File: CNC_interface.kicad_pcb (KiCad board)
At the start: 2 copper layers, 21 parts, among them J1 Conn_01x04_Male, J10 Conn_01x08, J11 Conn_01x08, J12 Conn_01x08, J13 Conn_01x08, J14 Conn_01x03_Male, J15 Conn_01x03_Male, J16 Conn_01x03_Male, J2 Conn_01x04_Male, J3 Conn_01x04_Male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

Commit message: adding capacitance footprints
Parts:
- added C1: CP, Capacitor_THT:CP_Radial_D8.0mm_P3.50mm, F.Cu at (214.6, 97.8)
- added C2: CP, Capacitor_THT:CP_Radial_D10.0mm_P5.00mm, F.Cu at (203.1, 98.8)

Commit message: Groupage drivers
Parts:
- moved J8 3.86 mm to (234.9, 69.9)
- moved J10 3.86 mm to (234.9, 95.9)
- moved J12 3.86 mm to (234.9, 121.3)
- moved J9 0.65 mm to (247.7, 69.9)
- moved J11 0.64 mm to (247.7, 95.9)
- moved J13 0.64 mm to (247.7, 121.3)
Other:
- net class Default removed

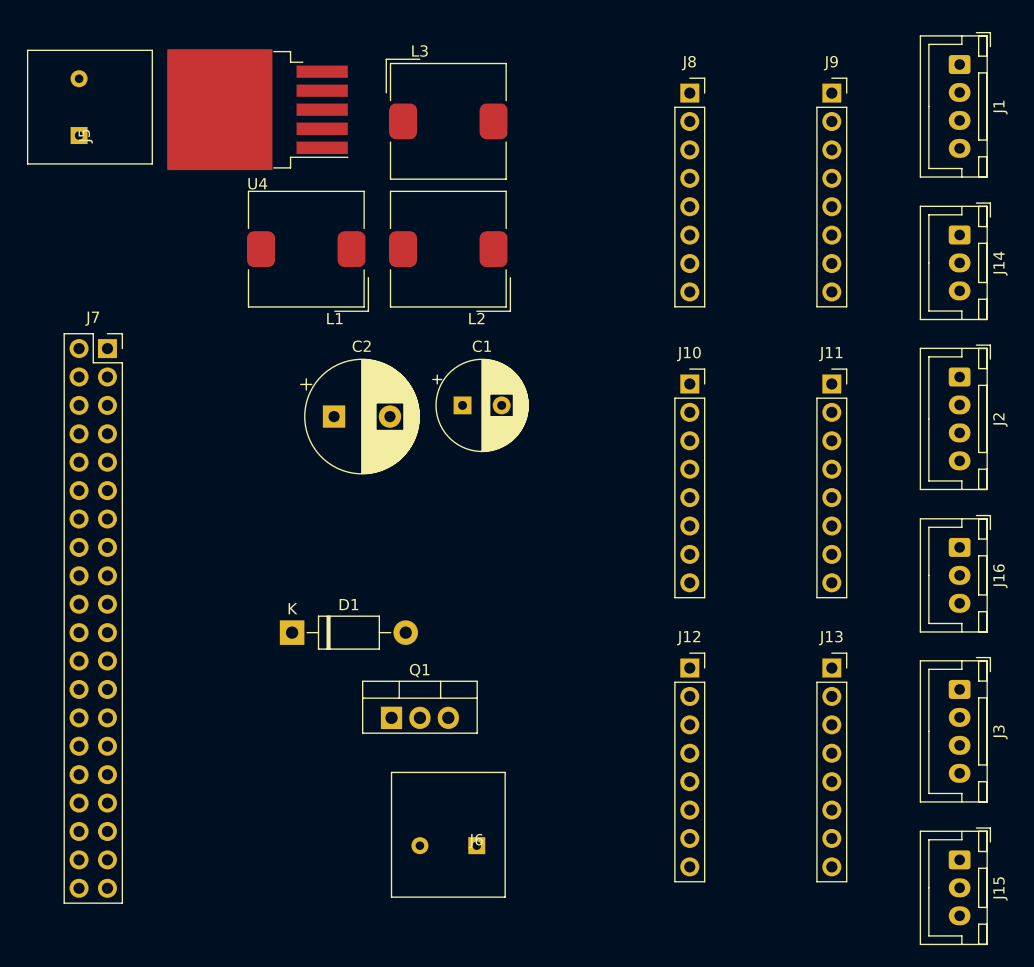
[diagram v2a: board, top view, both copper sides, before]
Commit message: Placing components on PCB
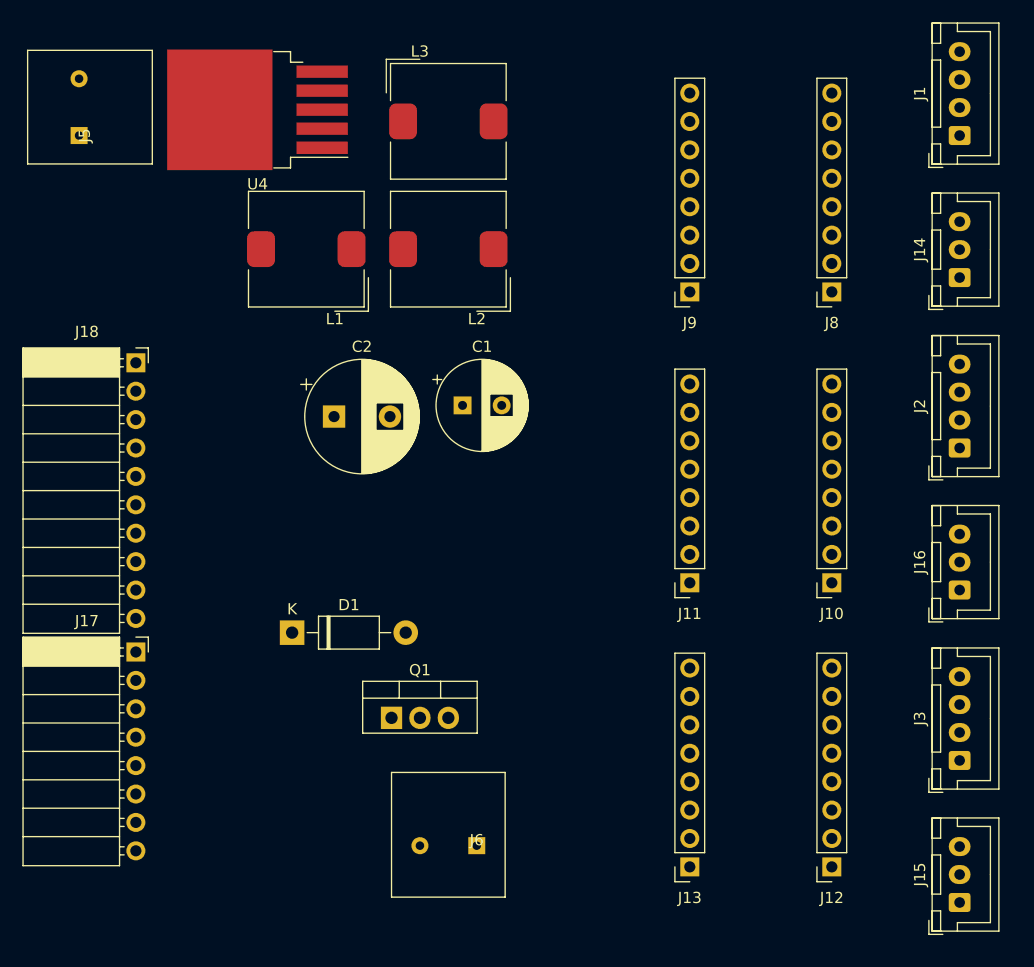
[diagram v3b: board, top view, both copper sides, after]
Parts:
- removed J7: Conn_02x20_Odd_Even, Connector_PinSocket_2.54mm:PinSocket_2x20_P2.54mm_Vertical
- added J17: Conn_01x08, Connector_PinSocket_2.54mm:PinSocket_1x08_P2.54mm_Horizontal, F.Cu at (185.4, 119.8)
- added J18: Conn_01x10, Connector_PinSocket_2.54mm:PinSocket_1x10_P2.54mm_Horizontal, F.Cu at (185.4, 94.0)
- moved J10 21.8 mm to (247.7, 113.7), turned to 180 degrees
- moved J11 21.8 mm to (234.9, 113.7), turned to 180 degrees
- moved J12 21.8 mm to (247.7, 139.1), turned to 180 degrees
- moved J13 21.8 mm to (234.9, 139.1), turned to 180 degrees
- moved J8 21.8 mm to (247.7, 87.6), turned to 180 degrees
- moved J9 21.8 mm to (234.9, 87.6), turned to 180 degrees
- moved J1 6.35 mm to (259.1, 73.7), turned to 90 degrees
- moved J2 6.35 mm to (259.1, 101.6), turned to 90 degrees
- moved J3 6.35 mm to (259.1, 129.5), turned to 90 degrees
- moved J14 3.81 mm to (259.1, 86.4), turned to 90 degrees
- moved J15 3.81 mm to (259.1, 142.2), turned to 90 degrees
- moved J16 3.81 mm to (259.1, 114.3), turned to 90 degrees
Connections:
- J1 pad 1: x1 -> OB2x
- J1 pad 2: x2 -> OB1x
- J1 pad 3: x3 -> OA1x
- J1 pad 4: x4 -> OA2x
- J10 pad 2: VIOy -> +5V
- J10 pad 8: VMy -> DC+
- J12 pad 2: VIOz -> +5V
- J12 pad 8: VMz -> DC+
- J2 pad 1: y1 -> OB2y
- J2 pad 2: y2 -> OB1y
- J2 pad 3: y3 -> OA1y
- J2 pad 4: y4 -> OA2y
- J3 pad 1: z1 -> OB2z
- J3 pad 2: z2 -> OB1z
- J3 pad 3: z3 -> OA1z
- J3 pad 4: z4 -> OA2z
- J8 pad 2: VIOx -> +5V
- J8 pad 8: VMx -> DC+

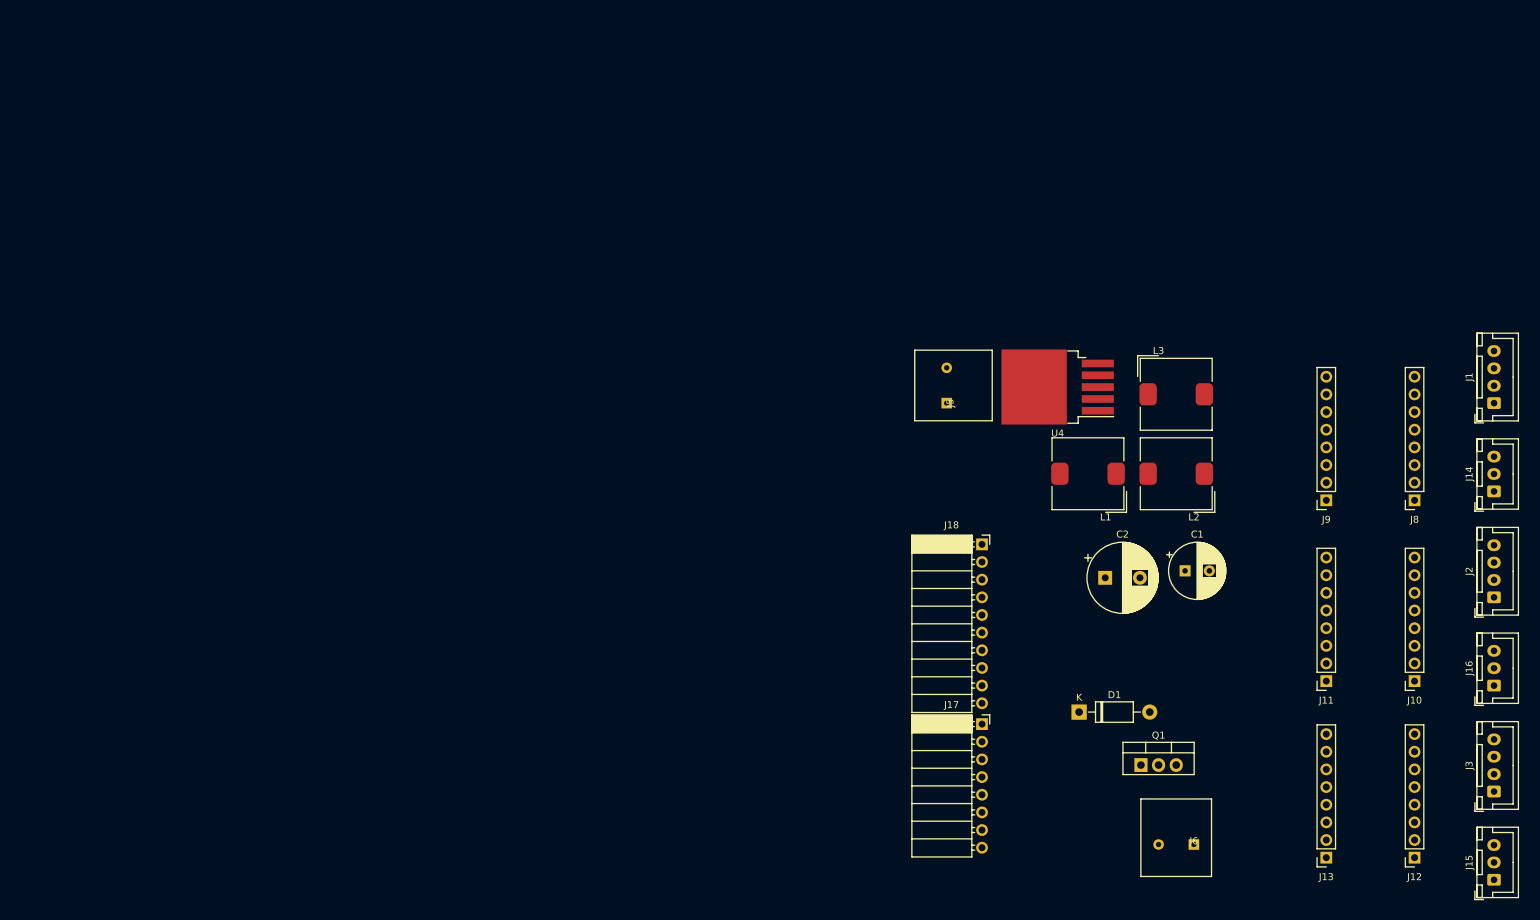
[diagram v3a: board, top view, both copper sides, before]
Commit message: wiring input to TMC
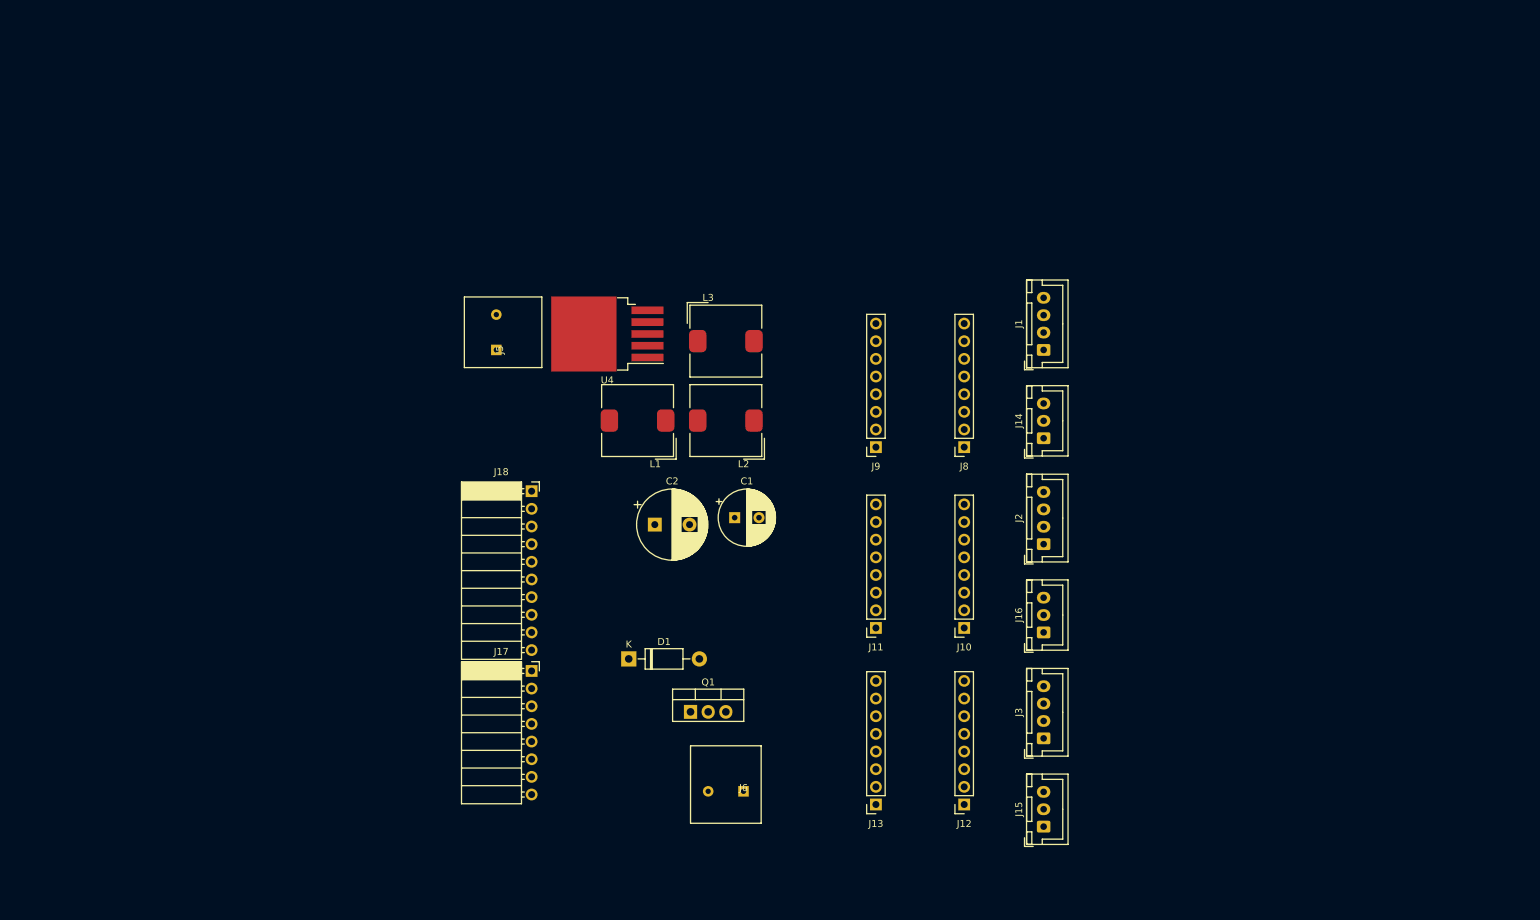
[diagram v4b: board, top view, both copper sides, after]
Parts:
- moved C2 65.2 mm to (138.3, 91.1)
- moved J10 65.2 mm to (182.9, 106.0)
- moved J12 65.2 mm to (182.9, 131.4)
- moved J6 65.2 mm to (151.1, 129.5)
- moved J8 65.2 mm to (182.9, 80.0)
- moved L2 65.2 mm to (148.6, 76.2)
- moved L3 65.2 mm to (148.6, 64.7)
- moved U4 65.2 mm to (131.5, 63.7)
- moved J5 65.2 mm to (115.5, 66.0)
- moved C1 65.2 mm to (149.8, 90.1)
- moved D1 65.2 mm to (134.6, 110.5)
- moved J1 65.2 mm to (194.3, 66.0)
- moved J11 65.2 mm to (170.2, 106.0)
- moved J13 65.2 mm to (170.2, 131.4)
- moved J14 65.2 mm to (194.3, 78.7)
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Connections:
- J11 pad 3: CLKy -> unconnected-(J11-Pad3)
- J11 pad 4: PDNUARTy -> unconnected-(J11-Pad4)
- J11 pad 5: PDNUARTy -> unconnected-(J11-Pad5)
- J13 pad 3: CLKz -> unconnected-(J13-Pad3)
- J13 pad 4: PDNUARTz -> unconnected-(J13-Pad4)
- J13 pad 5: PDNUARTz -> unconnected-(J13-Pad5)
- J17 pad 1: 7 -> ENy
- J17 pad 2: 6 -> STEPy
- J17 pad 3: 5 -> DIRy
- J17 pad 4: 4 -> ENx
- J17 pad 5: 3 -> STEPx
- J17 pad 6: 2 -> DIRx
- J18 pad 10: 8 -> DIRz
- J18 pad 6: 12 -> DCtrl
- J18 pad 8: 10 -> ENz
- J18 pad 9: 9 -> STEPz
- J9 pad 3: CLKx -> unconnected-(J9-Pad3)
- J9 pad 4: PDNUARTx -> unconnected-(J9-Pad4)
- J9 pad 5: PDNUARTx -> unconnected-(J9-Pad5)

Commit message: debut seance
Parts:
- added D2: D, Diode_THT:D_DO-201AD_P15.24mm_Horizontal, F.Cu at (119.3, 84.1)
- added J19: USB_C_Receptacle, Connector_USB:USB_C_Receptacle_Amphenol_12401548E4-2A_CircularHoles, F.Cu at (101.6, 113.6)
- moved J3 156.4 mm to (50.8, 59.8), turned to -90 degrees
- moved J1 150.6 mm to (50.8, 111.8), turned to -90 degrees
- moved J12 146.2 mm to (58.4, 54.6), turned to 0 degrees
- moved J2 143.8 mm to (50.8, 85.2), turned to -90 degrees
- moved J15 137.4 mm to (99.0, 35.6), turned to 180 degrees
- moved J6 132.3 mm to (50.8, 43.2), turned to 90 degrees
- moved J8 127.2 mm to (58.4, 106.7), turned to 0 degrees
- moved J10 127.1 mm to (58.4, 80.0), turned to 0 degrees
- moved J13 125.3 mm to (71.1, 54.6), turned to 0 degrees
- moved J14 116.3 mm to (86.2, 35.6), turned to 180 degrees
- moved Q1 113.1 mm to (63.5, 38.1), turned to -90 degrees
- moved J16 109.0 mm to (111.7, 35.6), turned to 180 degrees
- moved J9 102.5 mm to (71.1, 106.7), turned to 0 degrees
- moved J11 102.4 mm to (71.1, 80.0), turned to 0 degrees
- moved D1 94.6 mm to (73.7, 38.1), turned to -90 degrees
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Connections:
- net DC+ renamed +12V
- J14 pad 1: lx1 -> +5V
- J14 pad 2: lx2 -> GND
- J14 pad 3: lx3 -> Lx
- J15 pad 1: ly1 -> +5V
- J15 pad 2: ly2 -> GND
- J15 pad 3: ly3 -> Ly
- J16 pad 1: lz1 -> +5V
- J16 pad 2: lz2 -> GND
- J16 pad 3: lz3 -> Lz
- J17 pad 1: ENy -> STEPy
- J17 pad 2: STEPy -> DIRy
- J17 pad 3: DIRy -> ENx
- J17 pad 4: ENx -> STEPx
- J17 pad 5: STEPx -> DIRx
- J17 pad 6: DIRx -> Lx
- J17 pad 7: 1 -> Ly
- J17 pad 8: 0 -> Lz
- J18 pad 10: DIRz -> ENy
- J18 pad 7: 11 -> ENz
- J18 pad 8: ENz -> STEPz
- J18 pad 9: STEPz -> DIRz

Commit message: Starting routing & adding capa
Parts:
- moved J19 25.8 mm to (111.8, 137.2), turned to 0 degrees
- moved J18 1.43 mm to (51.6, 132.8)
- moved J17 1.43 mm to (77.5, 132.8)
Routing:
- net +12V: track 0.00 -> 31.1 mm
- net GND: track 0.00 -> 27.1 mm
- net Net-(D2-Pad1): track 0.00 -> 15.7 mm
- net OA2x: track 0.00 -> 7.69 mm
- net OA1x: track 0.00 -> 7.68 mm
- net OA2z: track 0.00 -> 7.68 mm
- net OA2y: track 0.00 -> 7.68 mm
- net OB2z: track 0.00 -> 7.66 mm
- net OB2y: track 0.00 -> 7.66 mm
- net OB1x: track 0.00 -> 7.66 mm
- net OA1z: track 0.00 -> 7.66 mm
- net OA1y: track 0.00 -> 7.66 mm
- net OB1y: track 0.00 -> 7.65 mm
- net OB1z: track 0.00 -> 7.65 mm
- net OB2x: track 0.00 -> 7.65 mm

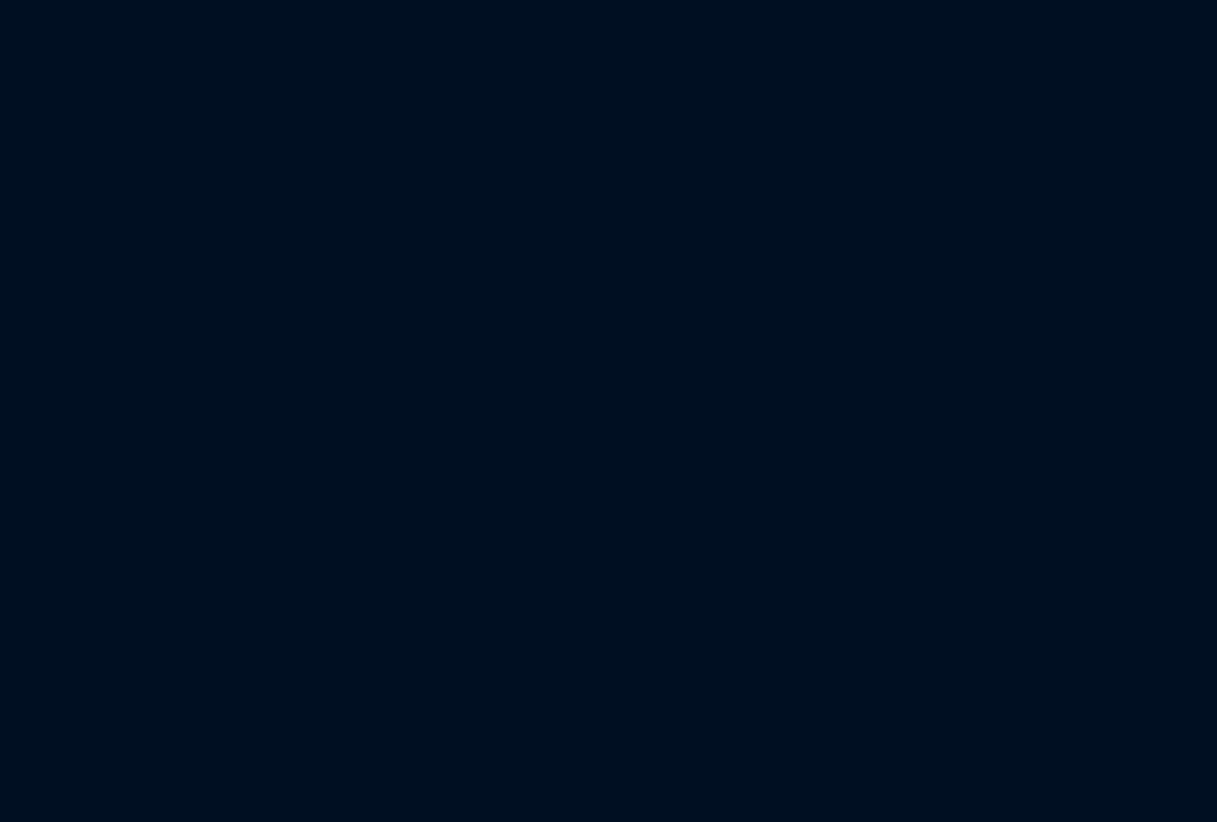
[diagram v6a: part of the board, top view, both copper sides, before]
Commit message: Add 12V power stage
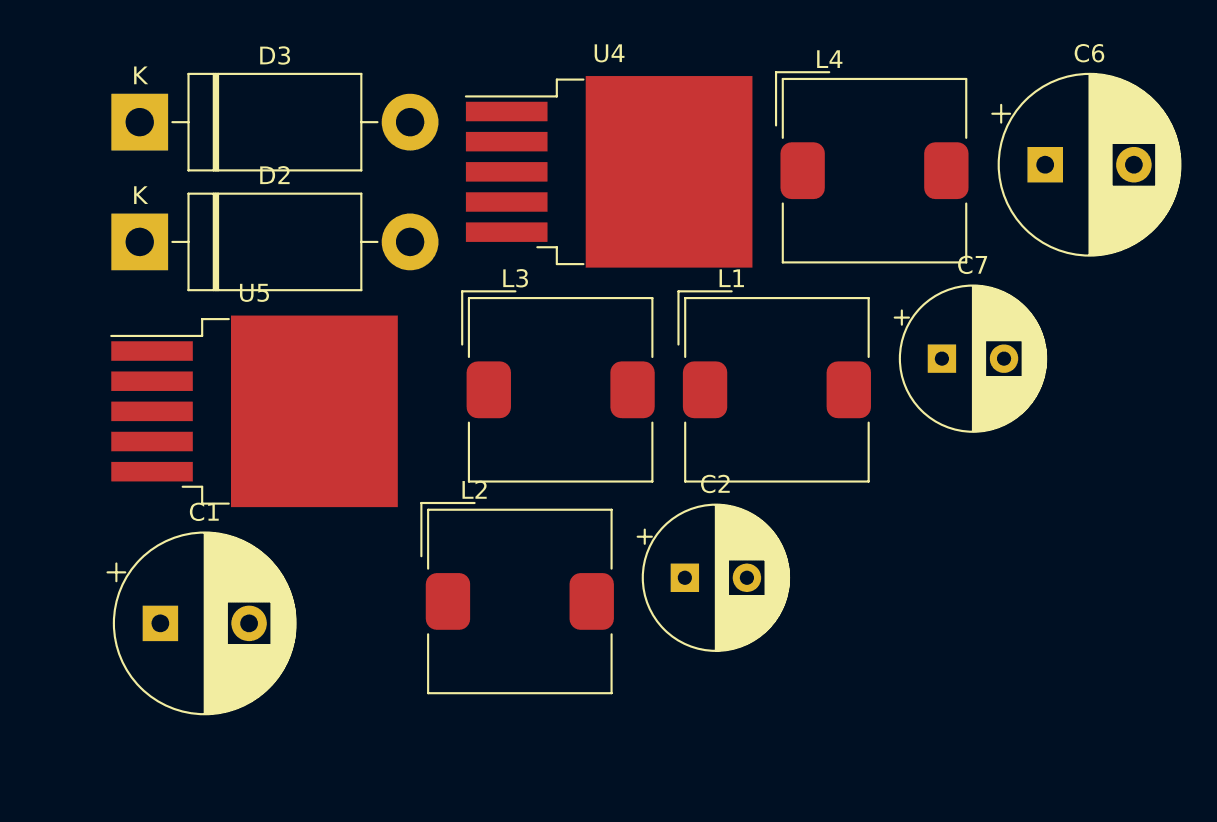
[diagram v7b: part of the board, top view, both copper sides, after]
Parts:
- added C1: CP, Capacitor_THT:CP_Radial_D10.0mm_P5.00mm, F.Cu at (129.5, 50.8)
- added C2: CP, Capacitor_THT:CP_Radial_D8.0mm_P3.50mm, F.Cu at (159.1, 48.2)
- added C6: CP, Capacitor_THT:CP_Radial_D10.0mm_P5.00mm, F.Cu at (179.4, 24.9)
- added C7: CP, Capacitor_THT:CP_Radial_D8.0mm_P3.50mm, F.Cu at (173.6, 35.9)
- added D2: D, Diode_THT:D_DO-201AD_P15.24mm_Horizontal, F.Cu at (128.4, 29.3)
- added D3: D, Diode_THT:D_DO-201AD_P15.24mm_Horizontal, F.Cu at (128.4, 22.6)
- added L1: L, Inductor_SMD:L_TDK_SLF10145, F.Cu at (164.3, 37.6)
- added L2: L, Inductor_SMD:L_TDK_SLF10145, F.Cu at (149.8, 49.6)
- added L3: L, Inductor_SMD:L_TDK_SLF10145, F.Cu at (152.1, 37.6)
- added L4: L, Inductor_SMD:L_TDK_SLF10145, F.Cu at (169.8, 25.3)
- added U4: LM2596S-5, Package_TO_SOT_SMD:TO-263-5_TabPin3, F.Cu at (154.8, 25.4)
- added U5: LM2596S-12, Package_TO_SOT_SMD:TO-263-5_TabPin3, F.Cu at (134.8, 38.9)
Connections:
- J10 pad 1: GND -> +5V
- J10 pad 7: GND -> +5V
- J11 pad 6: MS2y -> +5V
- J11 pad 7: MS1y -> unconnected-(J11-Pad7)
- J12 pad 1: GND -> +5V
- J12 pad 7: GND -> +5V
- J13 pad 6: MS2z -> unconnected-(J13-Pad6)
- J13 pad 7: MS1z -> unconnected-(J13-Pad7)
- J14 pad 2: GND -> +5V
- J15 pad 2: GND -> +5V
- J16 pad 2: GND -> +5V
- J18 pad 4: GND -> +5V
- J19 pad A1: GND -> +5V
- J19 pad A12: GND -> +5V
- J19 pad B1: GND -> +5V
- J19 pad B12: GND -> +5V
- J19 pad S1: GND -> +5V
- J5 pad 1: +12V -> +24V
- J5 pad 2: GND -> +5V
- J8 pad 1: GND -> +5V
- J8 pad 7: GND -> +5V
- J9 pad 6: MS2x -> +5V
- J9 pad 7: MS1x -> unconnected-(J9-Pad7)
- Q1 pad 3: GND -> +5V
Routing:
- net +24V: track 0.00 -> 31.1 mm
- net +12V: track 31.1 -> 0.00 mm
- net GND: track 27.1 -> 10.8 mm
- net +5V: track 0.00 -> 16.3 mm
